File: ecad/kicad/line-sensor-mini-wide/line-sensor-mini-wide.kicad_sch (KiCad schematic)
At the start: 37 parts, among them J1 SENSORS, Q1 BC337, Q2 BC337, Q3 BPW85C, Q4 BPW85C, Q5 BPW85C, Q6 BPW85C, Q7 BPW85C, Q8 BPW85C

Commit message: update line-sensor-mini-wide
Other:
- note added: "Indicator LEDs"
- note added: "Line Sensor Emitters"
- note added: "Marker Sensor Emitters"
- note added: "Mounting Holes"
- note added: "SENSOR CONNECTOR"
- note added: "Sensor Detectors"
- company: (none) -> UKMARS
- title: UKMARSBOT Template -> UKMARSBOT Line Sensor Mini
- moved on the sheet: D6, D7, R26, R27

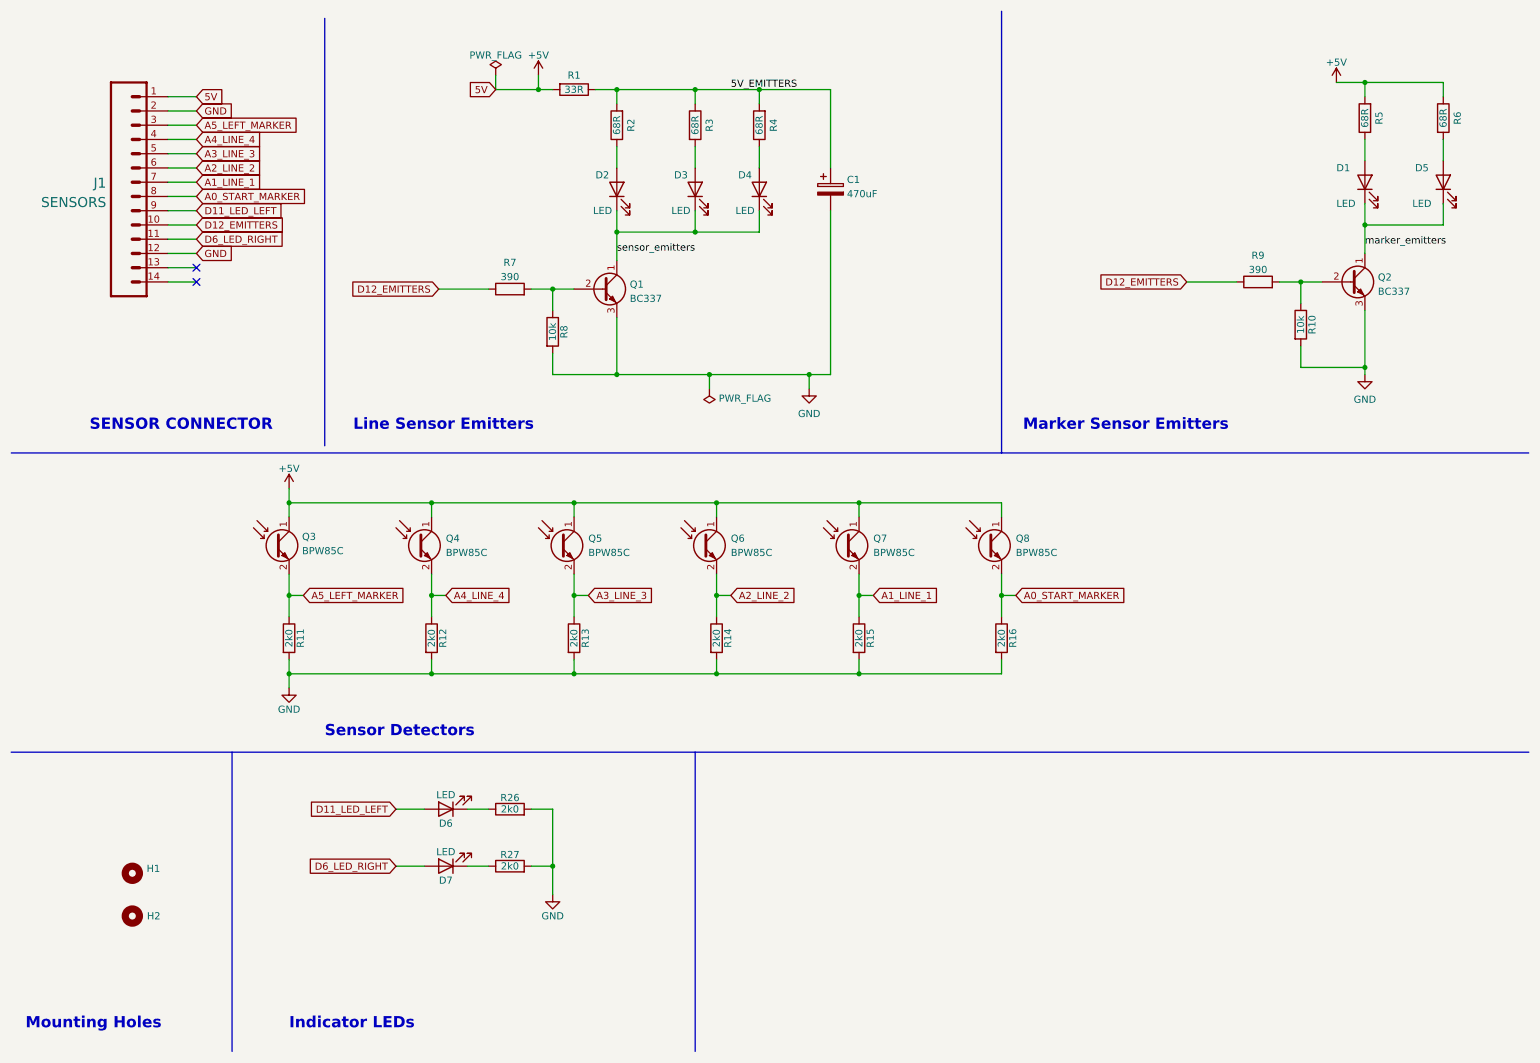
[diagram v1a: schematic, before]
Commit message: re-route mini wide line sensor
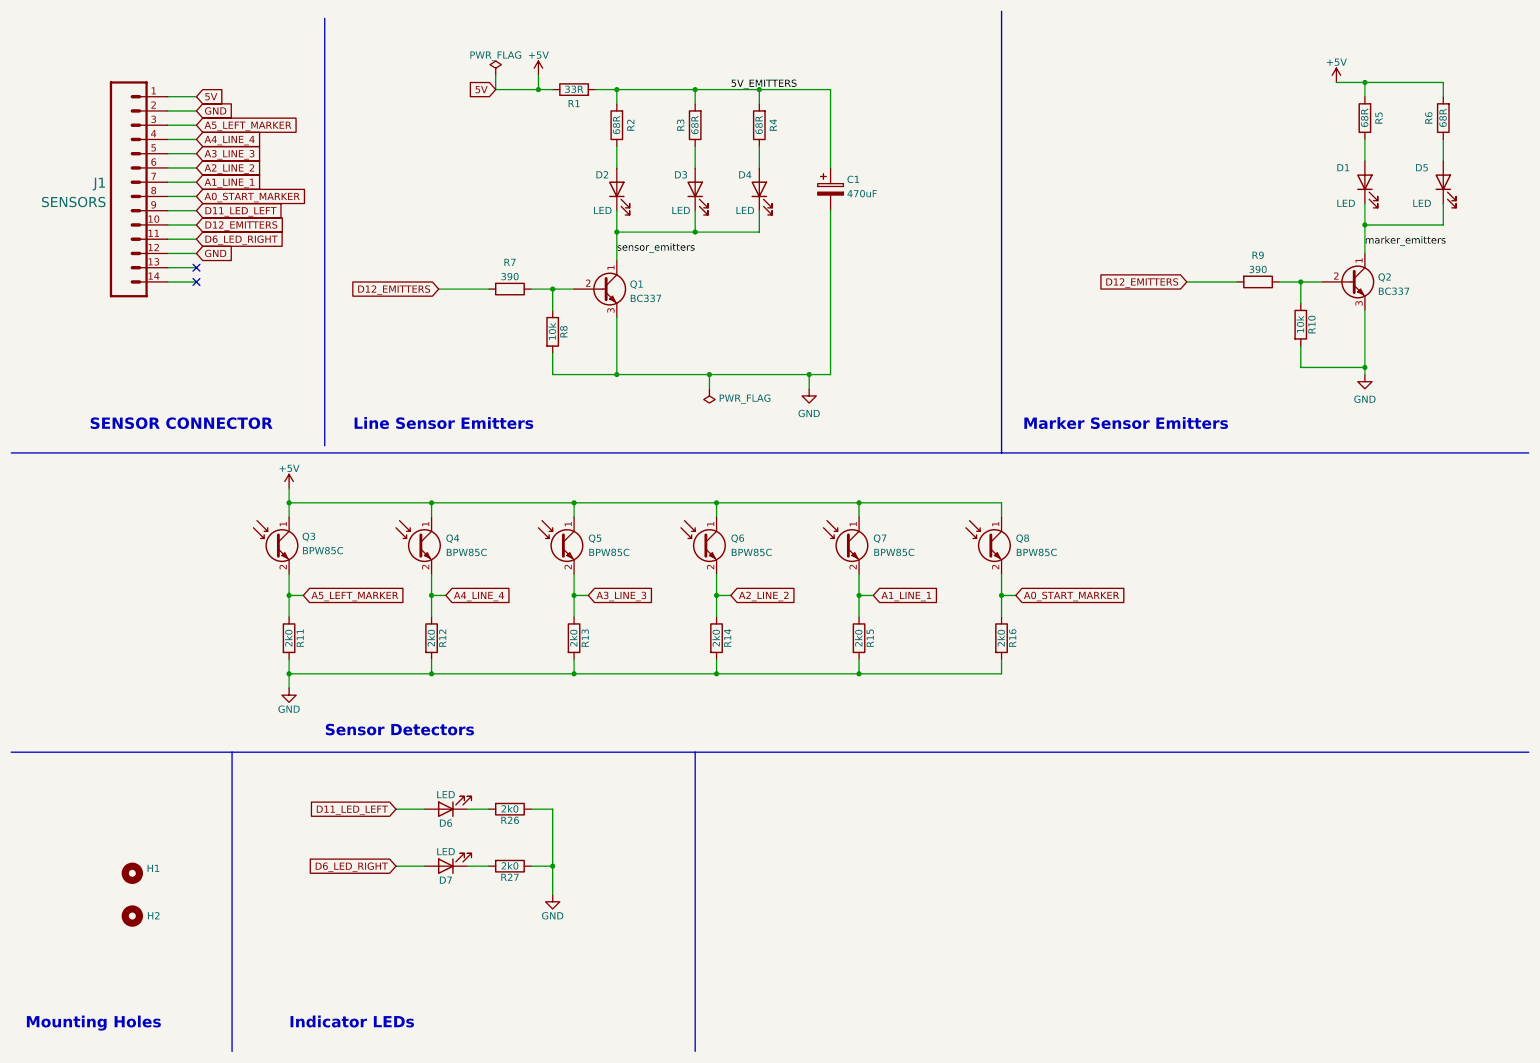
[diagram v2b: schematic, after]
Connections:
- net +5V: now also R1.1, R6.2; no longer R1.2, R6.1
- net 5V_EMITTERS: now also R1.2, R3.2; no longer R1.1, R3.1
- net D12_EMITTERS: now also R7.2, R9.2; no longer R7.1, R9.1
- net GND: now also R26.1, R27.1; no longer R26.2, R27.2
- net at Q2.2 (B), R10.1: now also R9.1; no longer R9.2
- net at D6.1 (K): now also R26.2; no longer R26.1
- net at Q1.2 (B), R8.1: now also R7.1; no longer R7.2
- net at D3.2 (A): now also R3.1; no longer R3.2
- net at D5.2 (A): now also R6.1; no longer R6.2
- net at D7.1 (K): now also R27.2; no longer R27.1
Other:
- moved on the sheet: R1, R26, R27, R3, R6, R7, R9
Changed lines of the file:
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@@
     (pin "2")
   )
-  (symbol (lib_id "Device:R") (at 236.22 59.69 90) (unit 1)
+  (symbol (lib_id "Device:R") (at 236.22 59.69 270) (unit 1)
     (in_bom yes) (on_board yes) (fields_autoplaced)
     (property "Reference" "R9" (id 0) (at 236.22 54.9742 90))
     (property "Value" "390" (id 1) (at 236.22 57.5111 90))
-    (property "Footprint" "Resistor_THT:R_Axial_DIN0207_L6.3mm_D2.5mm_P7.62mm_Horizontal" (id 2) (at 236.22 61.468 90)
+    (property "Footprint" "Resistor_THT:R_Axial_DIN0207_L6.3mm_D2.5mm_P7.62mm_Horizontal" (id 2) (at 236.22 57.912 90)
       (effects (font (size 1.27 1.27)) hide)
     )
@@
     (pin "2")
   )
-  (symbol (lib_id "Device:R") (at 102.87 153.67 90) (unit 1)
-    (in_bom yes) (on_board yes)
-    (property "Reference" "R26" (id 0) (at 102.87 151.638 90))
+  (symbol (lib_id "Device:R") (at 102.87 153.67 270) (unit 1)
+    (in_bom yes) (on_board yes)
+    (property "Reference" "R26" (id 0) (at 102.87 155.702 90))
     (property "Value" "2k0" (id 1) (at 102.87 153.67 90))
-    (property "Footprint" "Resistor_THT:R_Axial_DIN0207_L6.3mm_D2.5mm_P7.62mm_Horizontal" (id 2) (at 102.87 155.448 90)
+    (property "Footprint" "Resistor_THT:R_Axial_DIN0207_L6.3mm_D2.5mm_P7.62mm_Horizontal" (id 2) (at 102.87 151.892 90)
       (effects (font (size 1.27 1.27)) hide)
     )
@@
     (pin "2")
   )
-  (symbol (lib_id "Device:R") (at 114.3 25.4 270) (unit 1)
-    (in_bom yes) (on_board yes)
-    (property "Reference" "R1" (id 0) (at 114.3 22.86 90))
+  (symbol (lib_id "Device:R") (at 114.3 25.4 90) (unit 1)
+    (in_bom yes) (on_board yes)
+    (property "Reference" "R1" (id 0) (at 114.3 27.94 90))
     (property "Value" "33R" (id 1) (at 114.3 25.4 90))
-    (property "Footprint" "Resistor_THT:R_Axial_DIN0207_L6.3mm_D2.5mm_P7.62mm_Horizontal" (id 2) (at 114.3 23.622 90)
+    (property "Footprint" "Resistor_THT:R_Axial_DIN0207_L6.3mm_D2.5mm_P7.62mm_Horizontal" (id 2) (at 114.3 27.178 90)
       (effects (font (size 1.27 1.27)) hide)
     )
@@
     )
   )
-  (symbol (lib_id "Device:R") (at 135.89 31.75 0) (unit 1)
-    (in_bom yes) (on_board yes)
-    (property "Reference" "R3" (id 0) (at 138.43 31.75 90))
+  (symbol (lib_id "Device:R") (at 135.89 31.75 180) (unit 1)
+    (in_bom yes) (on_board yes)
+    (property "Reference" "R3" (id 0) (at 133.35 31.75 90))
     (property "Value" "68R" (id 1) (at 135.89 31.75 90))
-    (property "Footprint" "Resistor_THT:R_Axial_DIN0207_L6.3mm_D2.5mm_P7.62mm_Horizontal" (id 2) (at 134.112 31.75 90)
+    (property "Footprint" "Resistor_THT:R_Axial_DIN0207_L6.3mm_D2.5mm_P7.62mm_Horizontal" (id 2) (at 137.668 31.75 90)
       (effects (font (size 1.27 1.27)) hide)
     )
@@
     (pin "2")
   )
-  (symbol (lib_id "Device:R") (at 269.24 30.48 0) (unit 1)
-    (in_bom yes) (on_board yes)
-    (property "Reference" "R6" (id 0) (at 271.78 30.48 90))
+  (symbol (lib_id "Device:R") (at 269.24 30.48 180) (unit 1)
+    (in_bom yes) (on_board yes)
+    (property "Reference" "R6" (id 0) (at 266.7 30.48 90))
     (property "Value" "68R" (id 1) (at 269.24 30.48 90))
-    (property "Footprint" "Resistor_THT:R_Axial_DIN0207_L6.3mm_D2.5mm_P7.62mm_Horizontal" (id 2) (at 267.462 30.48 90)
+    (property "Footprint" "Resistor_THT:R_Axial_DIN0207_L6.3mm_D2.5mm_P7.62mm_Horizontal" (id 2) (at 271.018 30.48 90)
       (effects (font (size 1.27 1.27)) hide)
     )
@@
     (pin "2")
   )
-  (symbol (lib_id "Device:R") (at 102.87 163.83 90) (unit 1)
-    (in_bom yes) (on_board yes)
-    (property "Reference" "R27" (id 0) (at 102.87 161.798 90))
+  (symbol (lib_id "Device:R") (at 102.87 163.83 270) (unit 1)
+    (in_bom yes) (on_board yes)
+    (property "Reference" "R27" (id 0) (at 102.87 165.862 90))
     (property "Value" "2k0" (id 1) (at 102.87 163.83 90))
-    (property "Footprint" "Resistor_THT:R_Axial_DIN0207_L6.3mm_D2.5mm_P7.62mm_Horizontal" (id 2) (at 102.87 165.608 90)
+    (property "Footprint" "Resistor_THT:R_Axial_DIN0207_L6.3mm_D2.5mm_P7.62mm_Horizontal" (id 2) (at 102.87 162.052 90)
       (effects (font (size 1.27 1.27)) hide)
     )
@@
     )
   )
-  (symbol (lib_id "Device:R") (at 102.87 60.96 90) (unit 1)
+  (symbol (lib_id "Device:R") (at 102.87 60.96 270) (unit 1)
     (in_bom yes) (on_board yes) (fields_autoplaced)
     (property "Reference" "R7" (id 0) (at 102.87 56.2442 90))
     (property "Value" "390" (id 1) (at 102.87 58.7811 90))
-    (property "Footprint" "Resistor_THT:R_Axial_DIN0207_L6.3mm_D2.5mm_P7.62mm_Horizontal" (id 2) (at 102.87 62.738 90)
-      (effects (font (size 1.27 1.27)) hide)
-    )
+    (property "Footprint" "Resistor_THT:R_Axial_DIN0207_L6.3mm_D2.5mm_P7.62mm_Horizontal" (id 2) (at 102.87 59.182 90)
+      (effects (font (size 1.27 1.27)) hide)
+    )

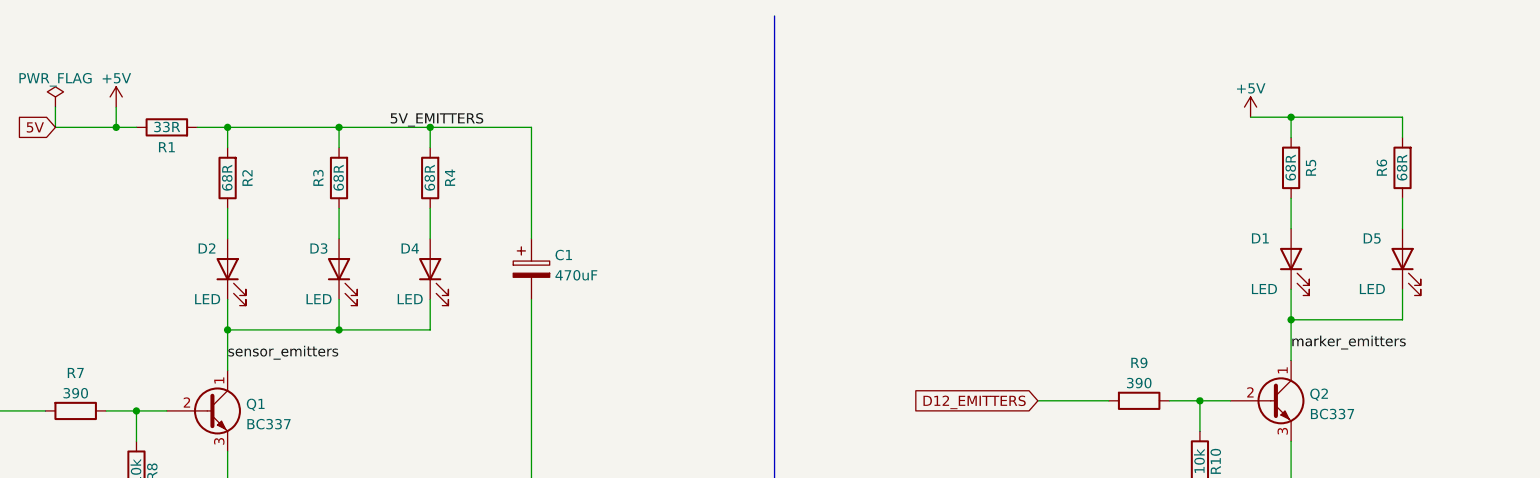
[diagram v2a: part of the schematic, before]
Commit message: improved BOM mini wide line sensor
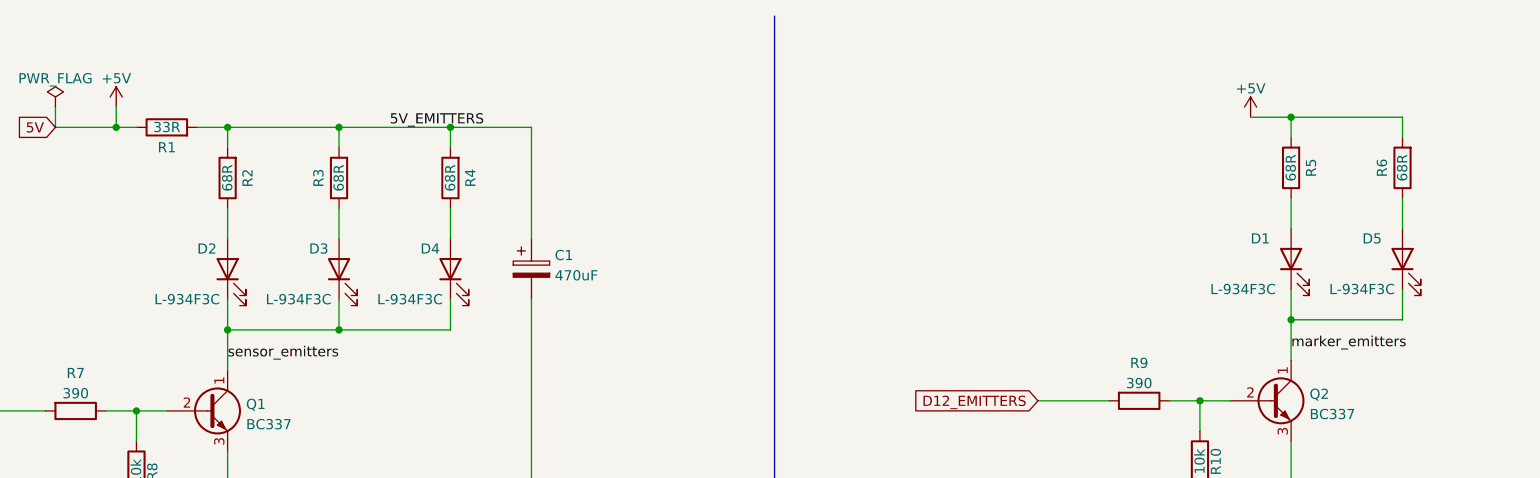
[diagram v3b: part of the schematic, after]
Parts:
- D1, D2, D3, D4, D5: value LED -> L-934F3C; Package (none) -> T-1 (3mm)
- D6, D7, Q3, Q4, Q5, Q6, Q7, Q8: Package (none) -> T-1 (3mm)
- H1, H2: Package (none) -> 3.2mm hole
- J1: Package (none) -> 14 pin 0.1" header
- Q1, Q2: Package (none) -> TO92
- R1, R10, R11, R12, R13, R14, R15, R16, R2, R26, R27, R3, R4, R5, R6, R7, R8, R9: Package (none) -> ¼ Watt, 0.3"
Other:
- moved on the sheet: D4, R4
